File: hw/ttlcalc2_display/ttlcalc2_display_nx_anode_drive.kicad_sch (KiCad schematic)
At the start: 89 parts, among them Q19 MPSA92, Q20 MPSA92, Q21 MPSA92, Q22 MPSA92, Q23 MPSA92, Q32 MPSA92, Q33 MPSA92, Q34 MPSA92, Q35 MPSA92, Q36 MPSA92, Q37 MPSA92, Q38 MPSA92, Q39 MPSA92, Q40 MPSA92, Q41 MPSA42, Q42 MPSA42, Q43 MPSA42, Q44 MPSA42, Q45 MPSA42, Q46 MPSA42, Q47 MPSA42, Q48 MPSA42, Q49 MPSA42, Q50 MPSA42, Q51 MPSA42, Q52 MPSA42, Q53 MPSA42, Q54 MPSA42, U13 74LS04, U14 74LS04, U15 74LS04, U2 74LS138, U3 74LS138

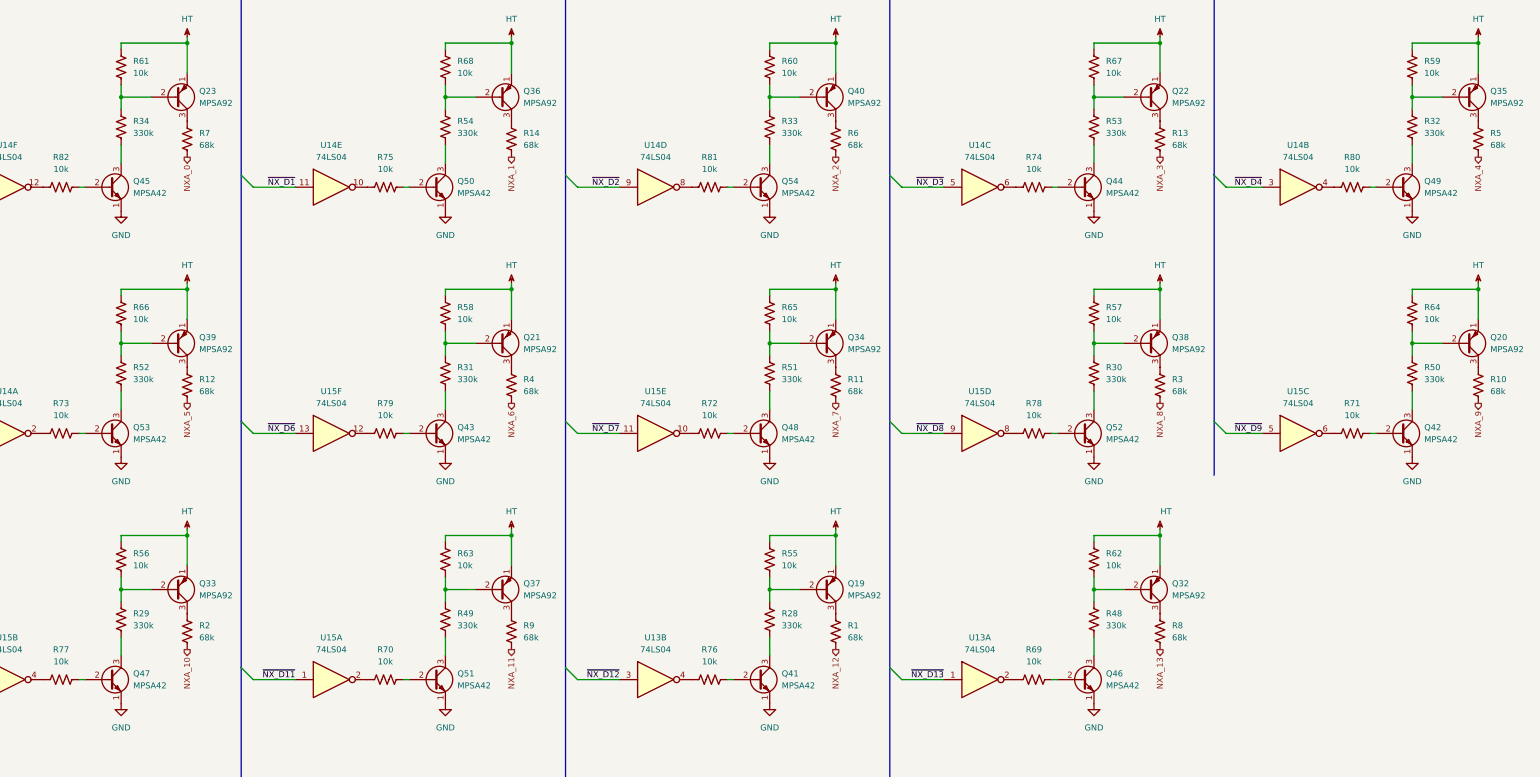
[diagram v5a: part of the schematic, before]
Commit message: Convert to KiCad 9.0
Convert to KiCad 9.0 format
Tweak silkscreen to fix DRC errors introduced by updated footprints
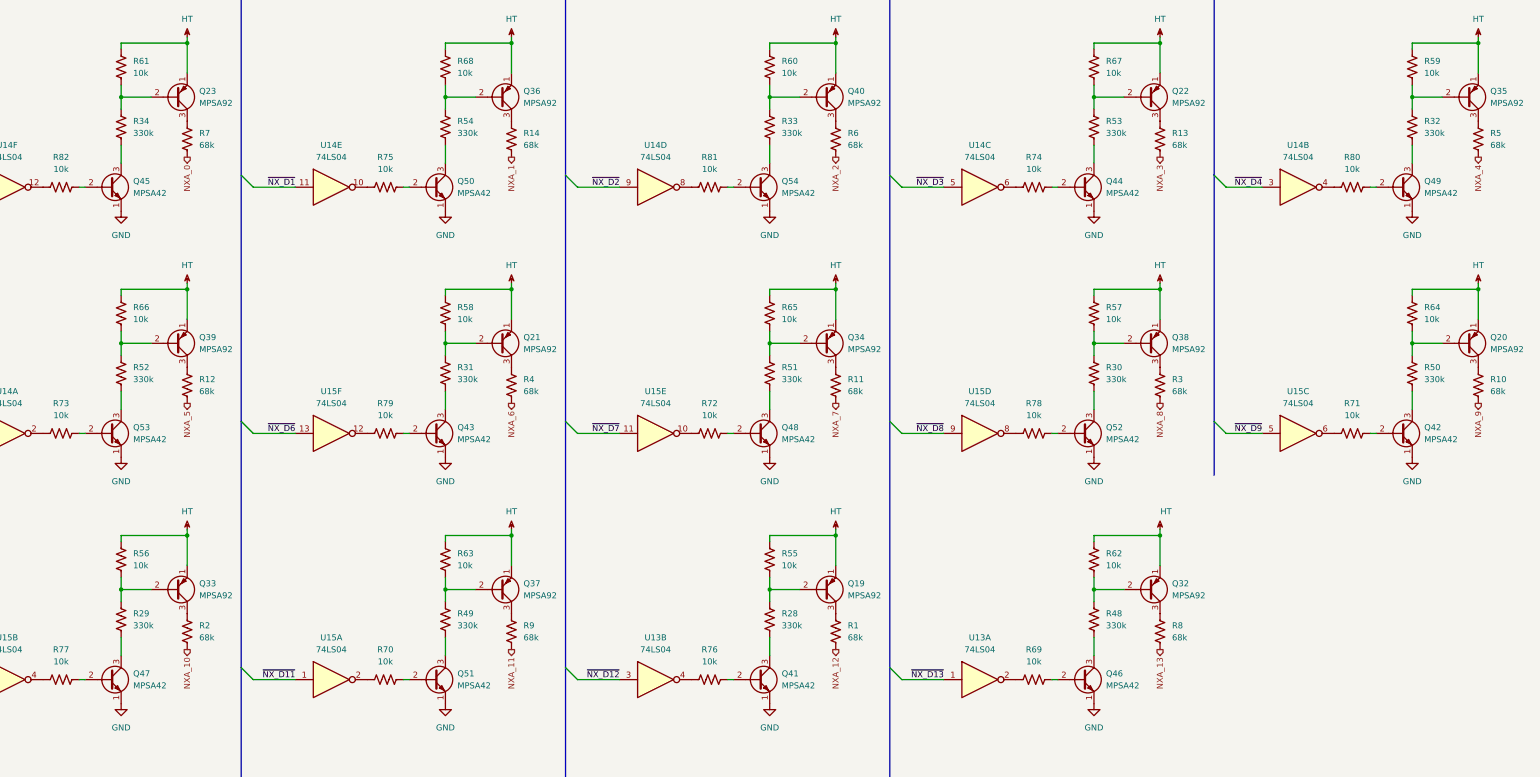
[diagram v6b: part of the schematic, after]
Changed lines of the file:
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@@
 (kicad_sch
-	(version 20231120)
+	(version 20250114)
 	(generator "eeschema")
-	(generator_version "8.0")
+	(generator_version "9.0")
 	(paper "USLedger")
 	(title_block
@@
 	(label "~{NX_D3}"
 		(at 295.91 115.57 180)
-		(fields_autoplaced yes)
 		(effects
 			(font
@@
 	(label "~{NX_D[0..13]}"
 		(at 163.83 72.39 0)
-		(fields_autoplaced yes)
 		(effects
 			(font
@@
 	(label "~{NX_D10}"
 		(at 90.17 219.71 180)
-		(fields_autoplaced yes)
 		(effects
 			(font
@@
 	(label "~{NX_D0}"
 		(at 90.17 115.57 180)
-		(fields_autoplaced yes)
 		(effects
 			(font
@@
 	(label "~{NX_D12}"
 		(at 227.33 219.71 180)
-		(fields_autoplaced yes)
 		(effects
 			(font
@@
 	(label "GND"
 		(at 40.64 96.52 180)
-		(fields_autoplaced yes)
 		(effects
 			(font
@@
 	(label "~{NX_D1}"
 		(at 158.75 115.57 180)
-		(fields_autoplaced yes)
 		(effects
 			(font
@@
 	(label "~{NX_D11}"
 		(at 158.75 219.71 180)
-		(fields_autoplaced yes)
 		(effects
 			(font
@@
 	(label "~{NX_D2}"
 		(at 66.04 35.56 0)
-		(fields_autoplaced yes)
 		(effects
 			(font
@@
 	(label "~{NX_D10}"
 		(at 66.04 83.82 0)
-		(fields_autoplaced yes)
 		(effects
 			(font
@@
 	(label "~{NX_D2}"
 		(at 227.33 115.57 180)
-		(fields_autoplaced yes)
 		(effects
 			(font
@@
 	(label "~{NX_D7}"
 		(at 227.33 167.64 180)
-		(fields_autoplaced yes)
 		(effects
 			(font
@@
 	(label "~{NX_D0}"
 		(at 66.04 30.48 0)
-		(fields_autoplaced yes)
 		(effects
 			(font
@@
 	(label "~{NX_D3}"
 		(at 66.04 38.1 0)
-		(fields_autoplaced yes)
 		(effects
 			(font
@@
 	(label "~{NX_D9}"
 		(at 66.04 81.28 0)
-		(fields_autoplaced yes)
 		(effects
 			(font
@@
 	(label "~{NX_D9}"
 		(at 363.22 167.64 180)
-		(fields_autoplaced yes)
 		(effects
 			(font
@@
 	(label "~{NX_D4}"
 		(at 363.22 115.57 180)
-		(fields_autoplaced yes)
 		(effects
 			(font
@@
 	(label "~{NX_D8}"
 		(at 295.91 167.64 180)
-		(fields_autoplaced yes)
 		(effects
 			(font
@@
 	(label "~{NX_D1}"
 		(at 66.04 33.02 0)
-		(fields_autoplaced yes)
 		(effects
 			(font
@@
 	(label "~{NX_D13}"
 		(at 66.04 91.44 0)
-		(fields_autoplaced yes)
 		(effects
 			(font
@@
 	(label "~{NX_D5}"
 		(at 90.17 167.64 180)
-		(fields_autoplaced yes)
 		(effects
 			(font
@@
 	(label "~{NX_D11}"
 		(at 66.04 86.36 0)
-		(fields_autoplaced yes)
 		(effects
 			(font
@@
 	(label "~{NX_D4}"
 		(at 66.04 40.64 0)
-		(fields_autoplaced yes)
 		(effects
 			(font
@@
 	(label "~{NX_D6}"
 		(at 66.04 45.72 0)
-		(fields_autoplaced yes)
 		(effects
 			(font
@@
 	(label "~{NX_D5}"
 		(at 66.04 43.18 0)
-		(fields_autoplaced yes)
 		(effects
 			(font
@@
 	(label "~{NX_D8}"
 		(at 66.04 78.74 0)
-		(fields_autoplaced yes)
 		(effects
 			(font
@@
 	(label "~{NX_D12}"
 		(at 66.04 88.9 0)
-		(fields_autoplaced yes)
 		(effects
 			(font
@@
 	(label "~{NX_D13}"
 		(at 295.91 219.71 180)
-		(fields_autoplaced yes)
 		(effects
 			(font
@@
 	(label "~{NX_D7}"
 		(at 66.04 48.26 0)
-		(fields_autoplaced yes)
 		(effects
 			(font
@@
 	(label "~{NX_D6}"
 		(at 158.75 167.64 180)
-		(fields_autoplaced yes)
 		(effects
 			(font
@@
 		(shape input)
 		(at 21.59 30.48 180)
-		(fields_autoplaced yes)
 		(effects
 			(font
@@
 		(shape input)
 		(at 21.59 33.02 180)
-		(fields_autoplaced yes)
 		(effects
 			(font
@@
 		(shape output)
 		(at 204.47 213.36 270)
-		(fields_autoplaced yes)
 		(effects
 			(font
@@
 		(shape output)
 		(at 135.89 109.22 270)
-		(fields_autoplaced yes)
 		(effects
 			(font
@@
 		(shape output)
 		(at 204.47 161.29 270)
-		(fields_autoplaced yes)
 		(effects
 			(font
@@
 		(shape output)
 		(at 273.05 213.36 270)
-		(fields_autoplaced yes)
 		(effects
 			(font
@@
 		(shape input)
 		(at 21.59 38.1 180)
-		(fields_autoplaced yes)
 		(effects
 			(font
@@
 		(shape input)
 		(at 21.59 35.56 180)
-		(fields_autoplaced yes)
 		(effects
 			(font
@@
 		(shape output)
 		(at 204.47 109.22 270)
-		(fields_autoplaced yes)
 		(effects
 			(font
@@
 		(shape output)
 		(at 135.89 213.36 270)
-		(fields_autoplaced yes)
 		(effects
 			(font
@@
 		(shape output)
 		(at 408.94 161.29 270)
-		(fields_autoplaced yes)
 		(effects
 			(font
@@
 		(shape output)
 		(at 273.05 109.22 270)
-		(fields_autoplaced yes)
 		(effects
 			(font
@@
 		(shape output)
 		(at 341.63 161.29 270)
-		(fields_autoplaced yes)
 		(effects
 			(font
@@
 		(shape output)
 		(at 135.89 161.29 270)
-		(fields_autoplaced yes)
 		(effects
 			(font
@@
 		(shape output)
 		(at 273.05 161.29 270)
-		(fields_autoplaced yes)
 		(effects
 			(font
@@
 		(shape output)
 		(at 408.94 109.22 270)
-		(fields_autoplaced yes)
 		(effects
 			(font
@@
 		(shape output)
 		(at 341.63 109.22 270)
-		(fields_autoplaced yes)
 		(effects
 			(font
@@
 		(shape output)
 		(at 341.63 213.36 270)
-		(fields_autoplaced yes)
 		(effects
 			(font
@@
 		(shape input)
 		(at 21.59 48.26 180)
-		(fields_autoplaced yes)
-		(effects
-			(font
+		(effects
+			(font

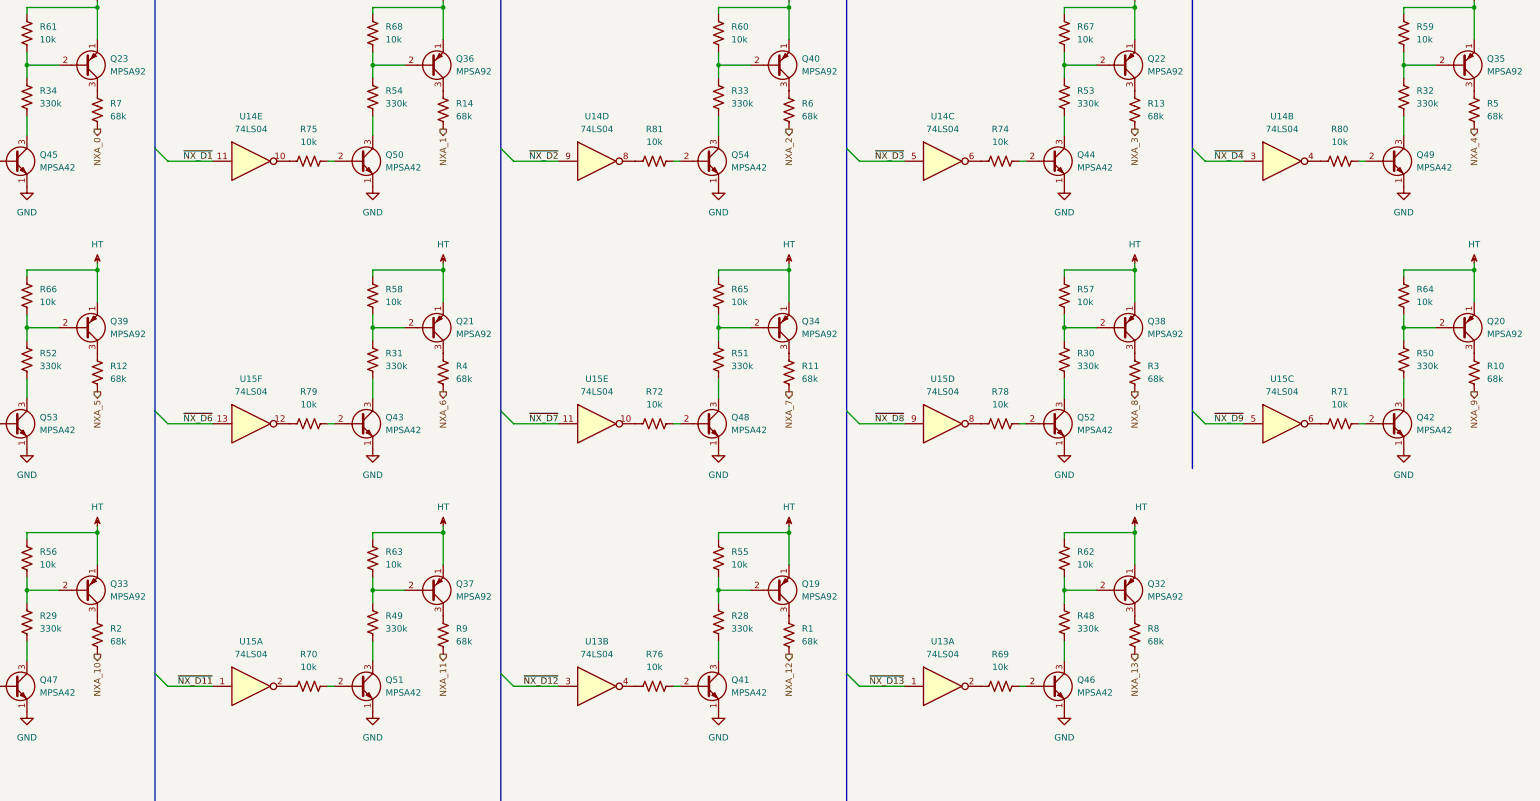
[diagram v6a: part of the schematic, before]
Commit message: Minor display hardware revisions
Add anti-ghosting inter-cathode resistors to nixies
Adjust component values based on experiments
Change from individual netclass labels to rule areas
Tweak traces on display board
Update .gitignore to ignore KiCad lock files
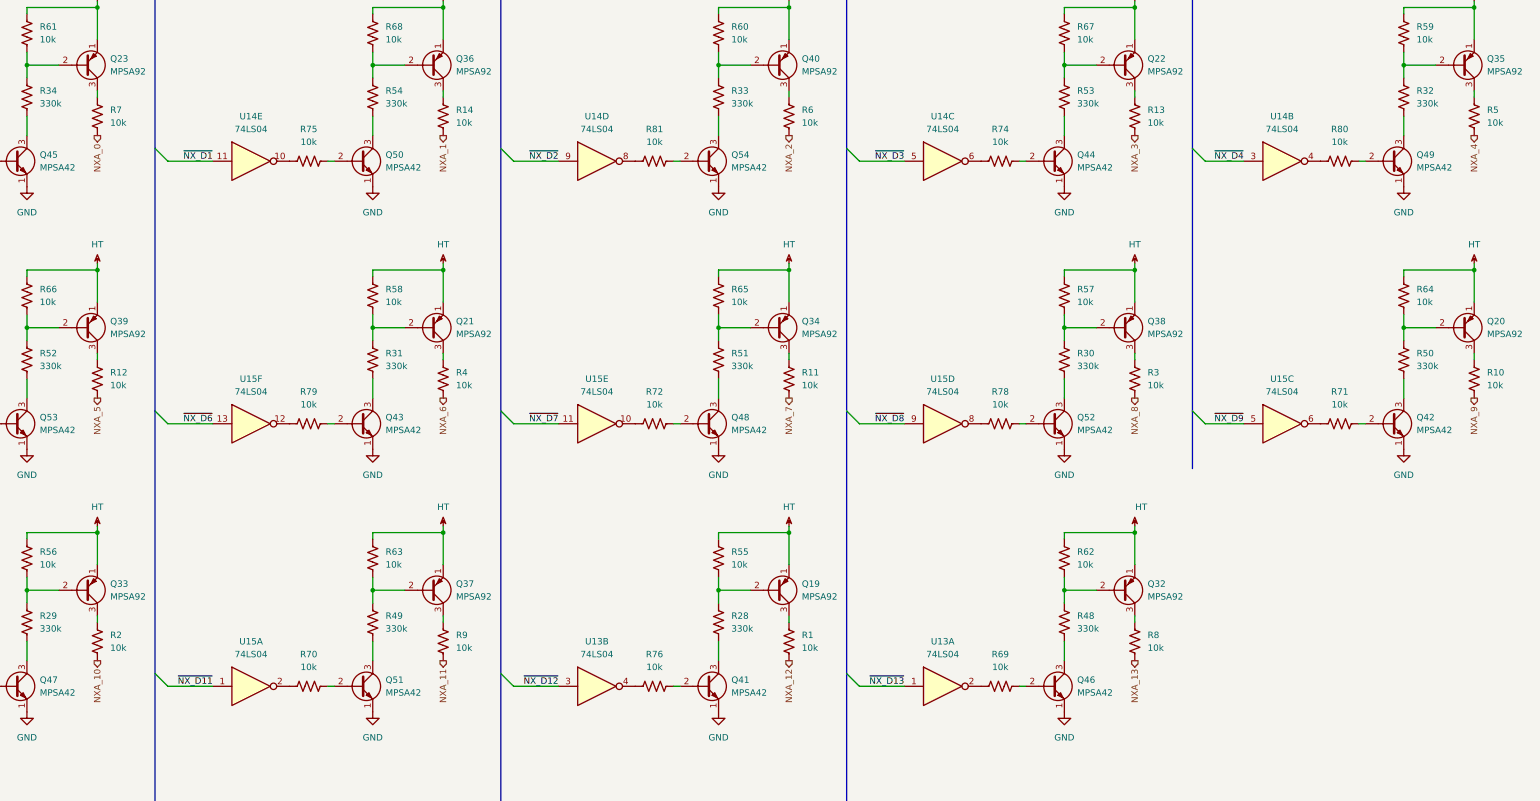
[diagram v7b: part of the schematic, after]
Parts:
- R1, R10, R11, R12, R13, R14, R2, R3, R4, R5, R6, R7, R8, R9: value 68k -> 10k
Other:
- moved on the sheet: R1, R10, R11, R12, R13, R14, R2, R3, R4, R5, R6, R7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

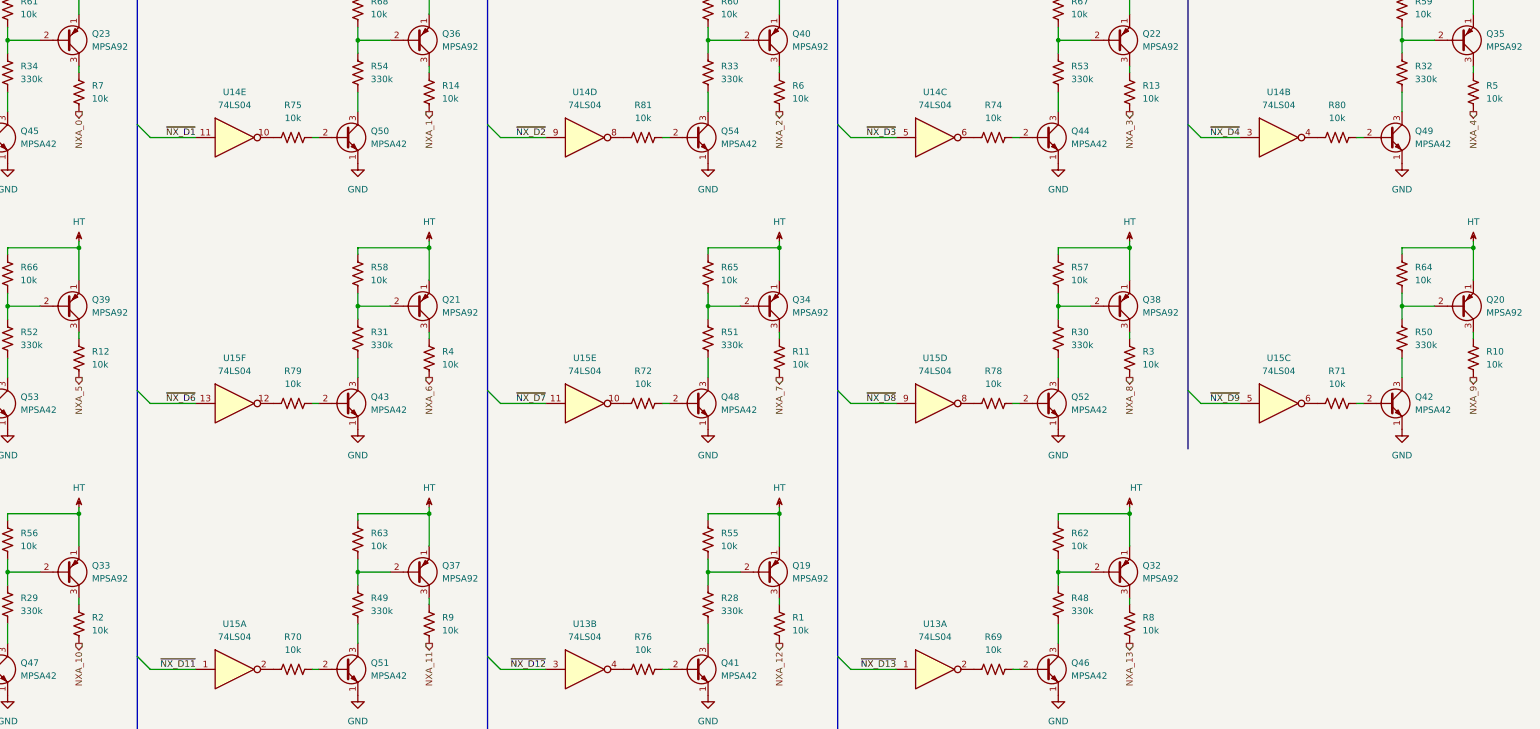
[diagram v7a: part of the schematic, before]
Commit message: More resistor value updates, ERC fixes
Update Nixie anode resistors to 22k based on calculation and experimental verification
Fix ERC errors due to remaining Logic netclass labels in decimal point sheet
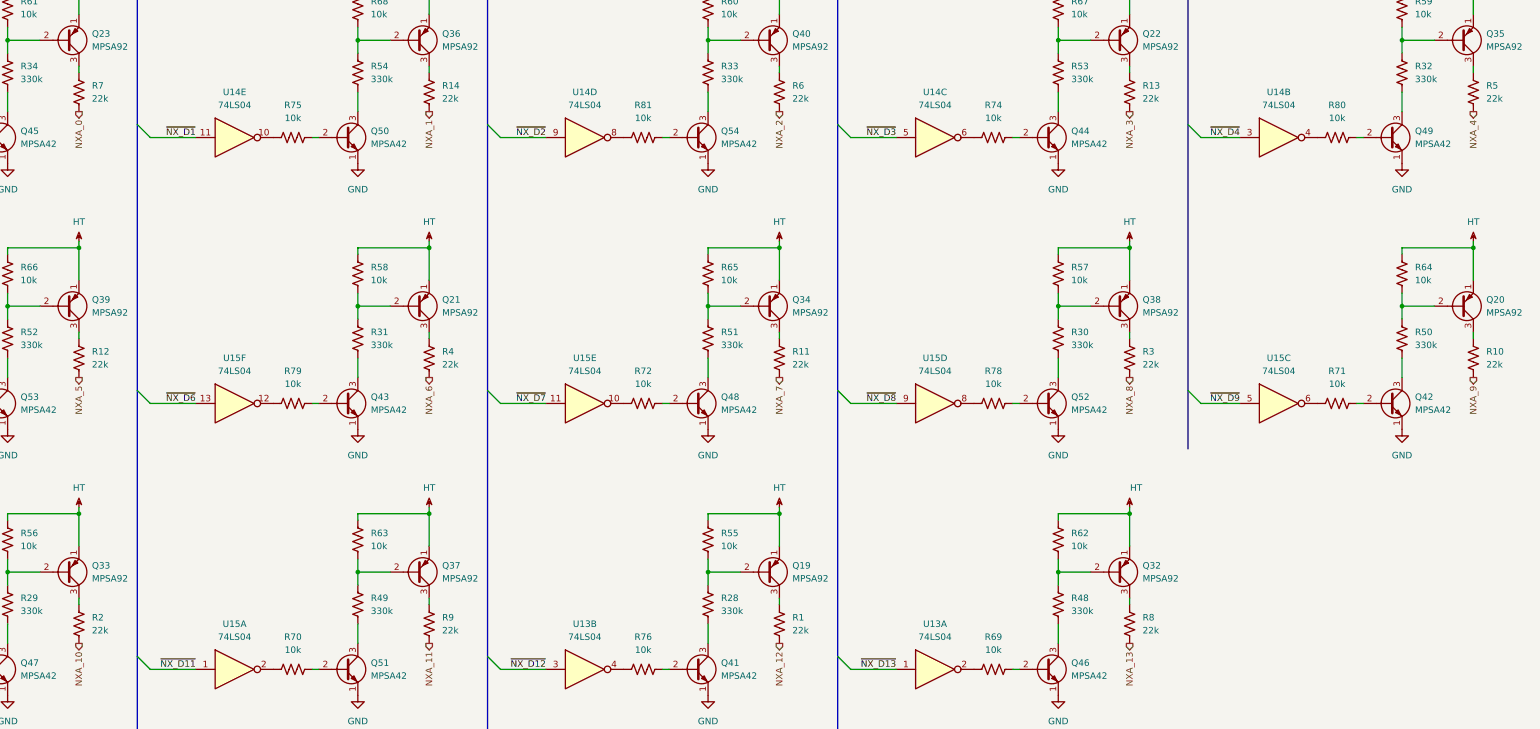
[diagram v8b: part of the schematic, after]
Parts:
- R1, R10, R11, R12, R13, R14, R2, R3, R4, R5, R6, R7, R8, R9: value 10k -> 22k
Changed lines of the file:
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@@
 			)
 		)
-		(property "Value" "10k"
+		(property "Value" "22k"
 			(at 275.59 212.0899 0)
 			(effects
@@
 			)
 		)
-		(property "Value" "10k"
+		(property "Value" "22k"
 			(at 207.01 160.0199 0)
 			(effects
@@
 			)
 		)
-		(property "Value" "10k"
+		(property "Value" "22k"
 			(at 344.17 160.0199 0)
 			(effects
@@
 			)
 		)
-		(property "Value" "10k"
+		(property "Value" "22k"
 			(at 207.01 212.0899 0)
 			(effects
@@
 			)
 		)
-		(property "Value" "10k"
+		(property "Value" "22k"
 			(at 411.48 160.0199 0)
 			(effects
@@
 			)
 		)
-		(property "Value" "10k"
+		(property "Value" "22k"
 			(at 138.43 212.0899 0)
 			(effects
@@
 			)
 		)
-		(property "Value" "10k"
+		(property "Value" "22k"
 			(at 138.43 107.9499 0)
 			(effects
@@
 			)
 		)
-		(property "Value" "10k"
+		(property "Value" "22k"
 			(at 411.48 107.9499 0)
 			(effects
@@
 			)
 		)
-		(property "Value" "10k"
+		(property "Value" "22k"
 			(at 275.59 107.9499 0)
 			(effects
@@
 			)
 		)
-		(property "Value" "10k"
+		(property "Value" "22k"
 			(at 138.43 160.0199 0)
 			(effects
@@
 			)
 		)
-		(property "Value" "10k"
+		(property "Value" "22k"
 			(at 207.01 107.9499 0)
 			(effects
@@
 			)
 		)
-		(property "Value" "10k"
+		(property "Value" "22k"
 			(at 344.17 212.0899 0)
 			(effects
@@
 			)
 		)
-		(property "Value" "10k"
+		(property "Value" "22k"
 			(at 275.59 160.0199 0)
 			(effects
@@
 			)
 		)
-		(property "Value" "10k"
+		(property "Value" "22k"
 			(at 344.17 107.9499 0)
 			(effects
